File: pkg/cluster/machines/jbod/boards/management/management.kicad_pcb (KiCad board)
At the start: 2 copper layers, 101 x 31.5 mm, 48 parts, among them J1 PSU_L, J10 FAN5, J11 FAN6, J12 I2C, J13 Conn_01x02, J2 FAN1, J3 SAS_L, J4 SAS_R, J5 LED, J6 PSU_R, J7 FAN2, J8 FAN3, J9 FAN4, Q1 2N7002, Q2 2N7002, Q3 DMG2301L, Q4 DMG2301L, U1 SN74AHCT125DR, U2 NRF52840_ITSY_BITSY, U3 AGQ20012

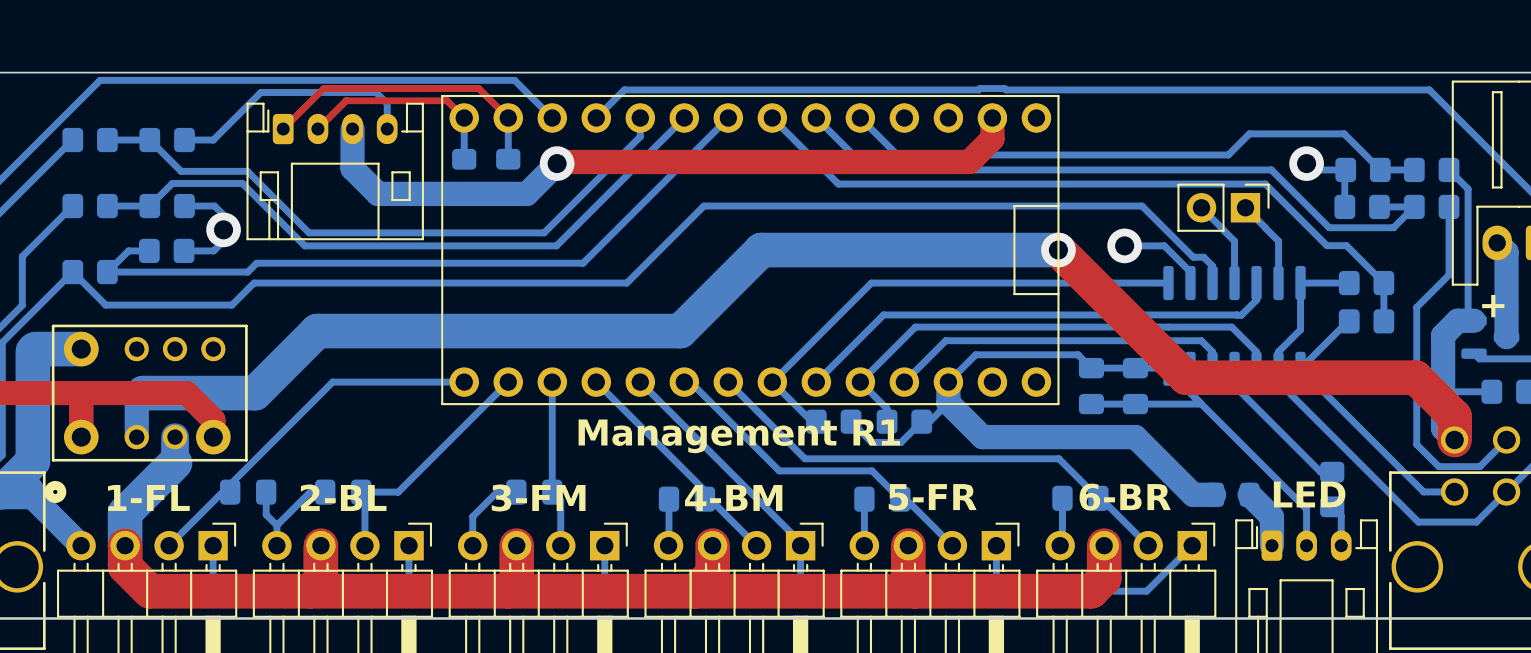
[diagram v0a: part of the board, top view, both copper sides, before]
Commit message: Add cluster blob replication and separate resolver service.
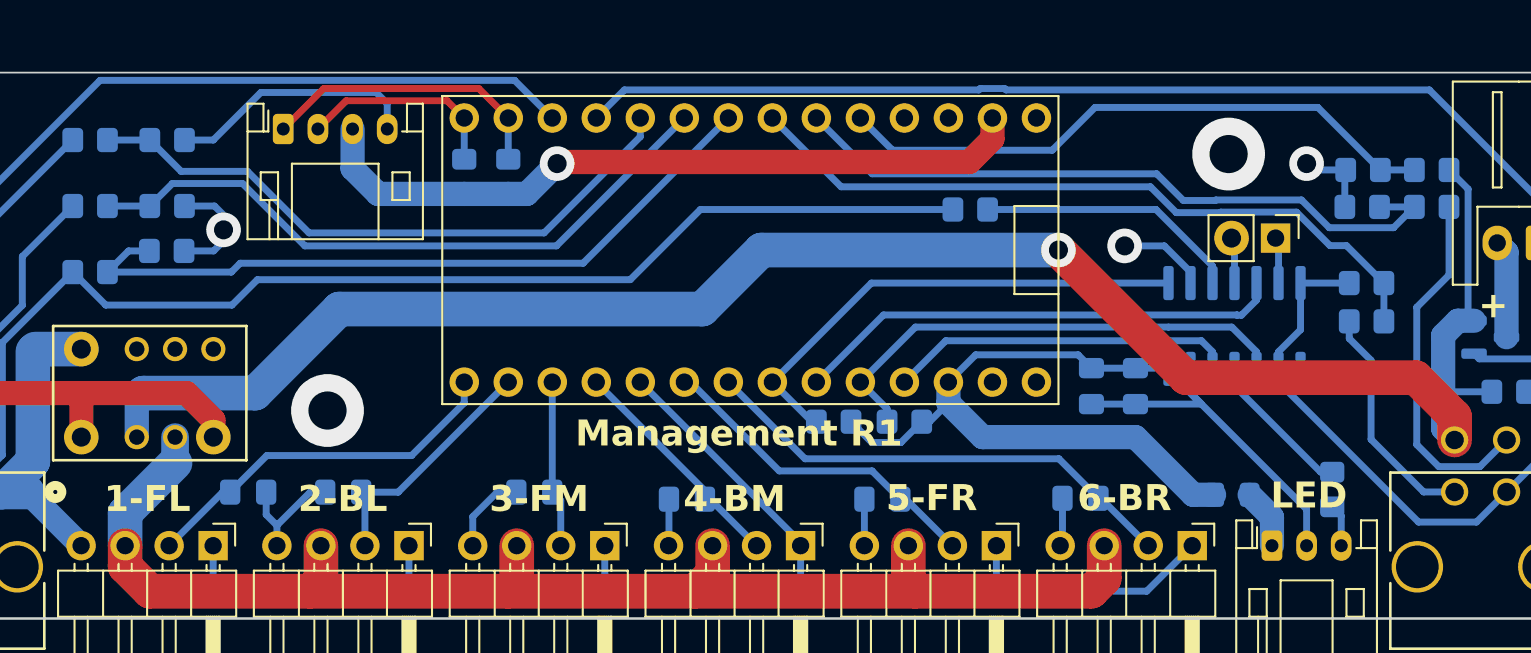
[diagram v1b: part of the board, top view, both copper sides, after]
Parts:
- added R20: 100, Resistor_SMD:R_0805_2012Metric_Pad1.20x1.40mm_HandSolder, B.Cu at (165.1, 76.4)
- added R21: 100, Resistor_SMD:R_0805_2012Metric_Pad1.20x1.40mm_HandSolder, B.Cu at (187.2, 86.3)
- moved J13 2.46 mm to (182.7, 78.0)
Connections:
- U1 pad 3: PS_ON_L_5V -> Net-(U1-1Y)
- U1 pad 8: PS_ON_R_5V -> Net-(U1-3Y)
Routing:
- net PS_ON_L_5V: track 88.8 -> 71.3 mm
- net Net-(U1-1Y): track 0.00 -> 15.3 mm
- net AUX_5V: track 5.13 -> 2.67 mm
- net GND: track 141.4 -> 138.9 mm, vias 3 -> 5
- net Net-(U1-3Y): track 0.00 -> 2.36 mm
- net PS_ON_R_5V: track 15.8 -> 13.5 mm
- net 12V_R_SENSE: track 34.2 -> 35.3 mm
- net FAN1_TACH: track 21.8 -> 22.5 mm

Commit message: Flushing some recent changes.
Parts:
- moved R15 3.04 mm to (133.2, 76.0)
- moved R20 1.60 mm to (165.0, 78.0)
- moved R14 1.50 mm to (138.4, 76.0)
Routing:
- net SDA: track 11.9 -> 18.5 mm, vias 0 -> 1
- net GND: track 138.9 -> 144.3 mm, vias 5 -> 6
- net 12V_L: track 50.8 -> 54.9 mm, vias 0 -> 2
- net SCL: track 17.0 -> 20.0 mm, vias 0 -> 1
- net +3.3V: track 42.3 -> 45.0 mm, vias 1 -> 2
- net 12V_R_SENSE: track 35.3 -> 36.9 mm
- net +5V: track 39.5 -> 40.7 mm
- net PS_ON_L_5V: track 71.3 -> 70.2 mm
- net 12V_R: track 107.7 -> 106.7 mm
- net PS_ON_R_SENSE: track 41.5 -> 42.0 mm
